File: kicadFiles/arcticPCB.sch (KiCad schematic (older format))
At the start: 174 parts, among them J1 TYPE-C-31-M12_13, J2 Conn_01x06_Male, J3 Conn_01x06_Male, J5 Conn_01x06_Male, SW1 MXSwitch, SW10 MXSwitch, SW11 MXSwitch, SW12 MXSwitch, SW13 MXSwitch, SW14 MXSwitch, SW15 MXSwitch, SW16 MXSwitch, SW17 MXSwitch, SW18 MXSwitch, SW19 MXSwitch, SW2 MXSwitch, SW20 MXSwitch, SW21 MXSwitch, SW22 MXSwitch, SW23 MXSwitch, SW24 MXSwitch, SW25 MXSwitch, SW26 MXSwitch, SW27 MXSwitch, SW28 MXSwitch, SW29 MXSwitch, SW3 MXSwitch, SW30 MXSwitch, SW31 MXSwitch, SW32 MXSwitch, SW33 MXSwitch, SW34 MXSwitch, SW35 MXSwitch, SW36 MXSwitch, SW37 MXSwitch, SW38 MXSwitch, SW39 MXSwitch, SW4 MXSwitch, SW40 MXSwitch, SW41 MXSwitch, SW42 MXSwitch, SW43 MXSwitch, SW44 MXSwitch, SW45 MXSwitch, SW46 MXSwitch, SW47 MXSwitch, SW48 MXSwitch, SW49 MXSwitch, SW5 MXSwitch, SW50 MXSwitch, SW51 MXSwitch, SW52 MXSwitch, SW53 MXSwitch, SW54 MXSwitch, SW55 MXSwitch, SW56 MXSwitch, SW57 MXSwitch, SW58 MXSwitch, SW59 MXSwitch, SW6 MXSwitch, SW60 MXSwitch, SW61 MXSwitch, SW62 MXSwitch, SW63 MXSwitch, SW64 MXSwitch, SW65 MXSwitch, SW7 MXSwitch, SW8 MXSwitch, SW9 MXSwitch, U1 STM32F072-LQFP48, U2 USBLC6-2SC6, U3 MCP1700-3302E_SOT23

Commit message: Add extra pins, organize schematic, add renders
- There were two pins in the PCB that were left unused and un-exposed to use. Now those two pins are broken out so they can be used. To execute this, some cols and rows had to have their pins reallocated.

- Schematic is better organized;

- Added KLE and PCB renders at the REAME file.
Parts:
- added J4: Conn_01x02, Connector_PinHeader_2.54mm:PinHeader_1x02_P2.54mm_Vertical, symbol Connector_Generic:Conn_01x02
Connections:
- net Col10: now also U1.4 (PC15/OSC32_OUT); no longer U1.3 (PC14/OSC32_IN)
- net Col11: now also U1.3 (PC14/OSC32_IN); no longer U1.2 (PC13)
- net Col12: now also U1.2 (PC13); no longer U1.46 (SPI2_NSS/I2S2_WS/I2C1_SDA/TIM17_CH1/PB9)
- net Col13: now also U1.46 (SPI2_NSS/I2S2_WS/I2C1_SDA/TIM17_CH1/PB9); no longer U1.45 (I2C1_SCL/TIM16_CH1/PB8)
- net Col14: now also U1.45 (I2C1_SCL/TIM16_CH1/PB8); no longer U1.43 (2C1_SDA/PB7)
- net Row1: now also U1.43 (2C1_SDA/PB7); no longer U1.42 (I2C1_SCL/PB6)
- net Row2: now also U1.42 (I2C1_SCL/PB6); no longer U1.41 (SPI1_MOSI/I2S1_SD/TIM3_CH2/PB5)
- net J4_2: now reaches U1.40 (SPI1_MISO/I2S1_MCK/TIM3_CH1/PB4)
- net J4_2: now also J4.2 (Pin_2)
- new net J4_1: J4.1 (Pin_1), U1.41 (SPI1_MOSI/I2S1_SD/TIM3_CH2/PB5)
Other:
- note added: "Mounting holes"
- note added: "Switch matrix"
- moved on the sheet: CB1, CB2, CB3, CB4, CB5, CB6, CB7, CB8, H8, L1, L2, L3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

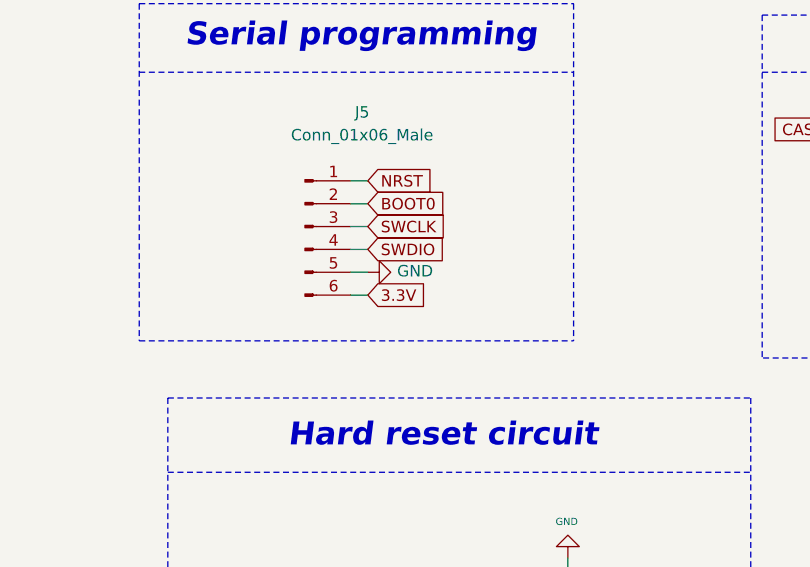
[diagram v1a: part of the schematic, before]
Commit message: Optimize routing, move SWD pins
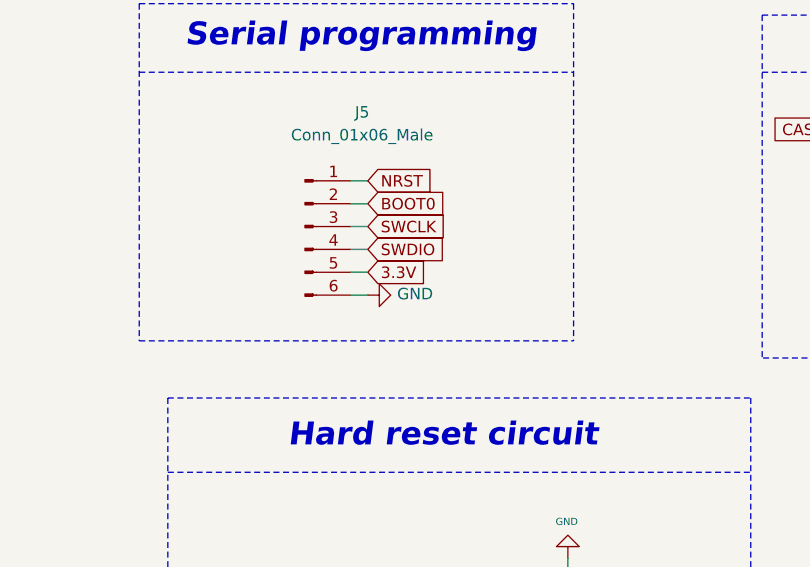
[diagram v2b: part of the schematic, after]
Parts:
- SW1, SW10, SW11, SW12, SW13, SW16, SW17, SW18, SW19, SW2, SW20, SW21, SW22, SW23, SW24, SW25, SW26, SW27, SW3, SW30, SW31, SW32, SW33, SW34, SW35, SW36, SW37, SW38, SW39, SW4, SW40, SW43, SW44, SW45, SW46, SW47, SW48, SW49, SW5, SW50, SW51, SW52, SW55, SW59, SW6, SW61, SW64, SW65, SW7, SW8, SW9: footprint acheron_MX:MX100 -> acheron_MX_SolderMask:MX100
- SW14: footprint acheron_MX:MX200 -> acheron_MX_SolderMask:MX200
- SW15, SW28, SW54, SW56, SW58, SW60: footprint acheron_MX:MX150 -> acheron_MX_SolderMask:MX150
- SW29, SW62: footprint acheron_MX:MX175 -> acheron_MX_SolderMask:MX175
- SW41, SW42: footprint acheron_MX:MX225 -> acheron_MX_SolderMask:MX225
- SW53: footprint acheron_MX:MX275 -> acheron_MX_SolderMask:MX275
- SW57: footprint acheron_MX:MX700R -> acheron_MX_SolderMask:MX700R
- SW63: footprint acheron_MX:MX125 -> acheron_MX_SolderMask:MX125
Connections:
- net 3.3V: now also J5.5 (Pin_5); no longer J5.6 (Pin_6)
- net GND: now also J5.6 (Pin_6); no longer J5.5 (Pin_5)

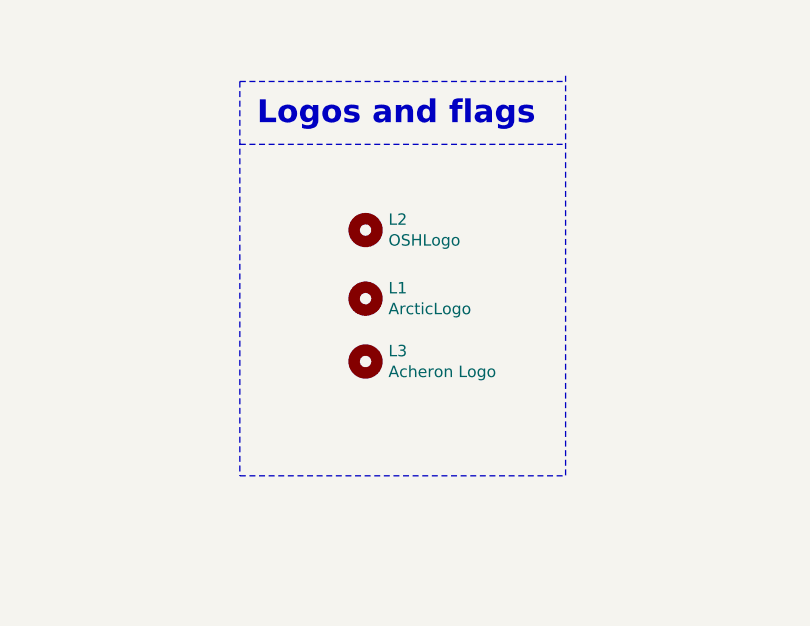
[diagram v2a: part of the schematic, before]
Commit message: Reorganize graphics, optimize routing
- The ./graphics folder was reorganized

- Some traces, specially the ones leading to SWD pins, were re-done for
efficiency and optimization
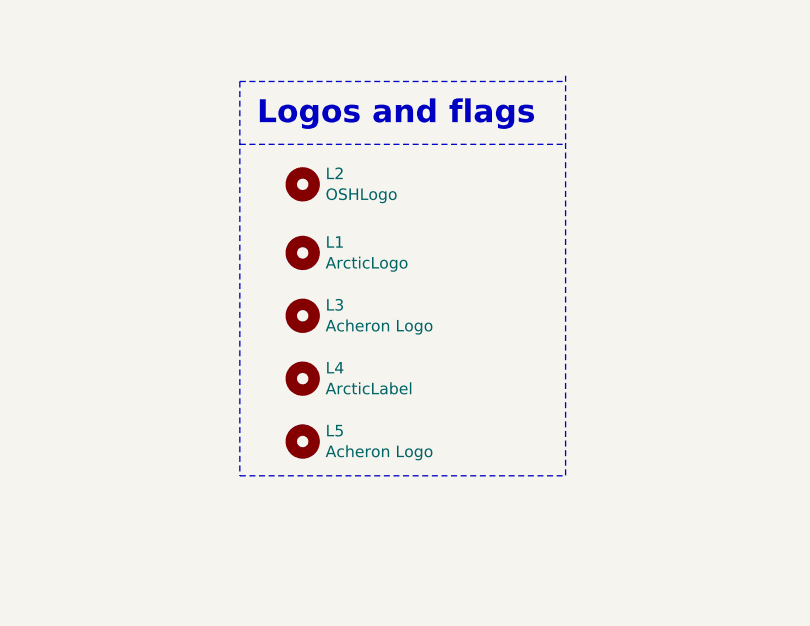
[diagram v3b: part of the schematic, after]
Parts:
- added L4: ArcticLabel, arcticGraphics:arcticLabel, symbol Mechanical:MountingHole
- added L5: Acheron Logo, arcticGraphics:arcticLabelMask, symbol Mechanical:MountingHole
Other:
- moved on the sheet: L1, L2, L3
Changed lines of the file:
@@
 L Mechanical:MountingHole L2
 U 1 1 5C66B5D5
-P 3000 14725
-F 0 "L2" H 3100 14771 50  0000 L CNN
-F 1 "OSHLogo" H 3100 14680 50  0000 L CNN
-F 2 "oshLogo:osh-logo" H 3000 14725 50  0001 C CNN
-F 3 "~" H 3000 14725 50  0001 C CNN
-	1    3000 14725
+P 2725 14525
+F 0 "L2" H 2825 14571 50  0000 L CNN
+F 1 "OSHLogo" H 2825 14480 50  0000 L CNN
+F 2 "oshLogo:osh-logo" H 2725 14525 50  0001 C CNN
+F 3 "~" H 2725 14525 50  0001 C CNN
+	1    2725 14525
 	1    0    0    -1
 $EndComp
@@
 L Mechanical:MountingHole L1
 U 1 1 5D3B6D2E
-P 3000 15025
-F 0 "L1" H 3100 15071 50  0000 L CNN
-F 1 "ArcticLogo" H 3100 14980 50  0000 L CNN
-F 2 "arcticLogo:arcticLogoFilled" H 3000 15025 50  0001 C CNN
-F 3 "~" H 3000 15025 50  0001 C CNN
-	1    3000 15025
+P 2725 14825
+F 0 "L1" H 2825 14871 50  0000 L CNN
+F 1 "ArcticLogo" H 2825 14780 50  0000 L CNN
+F 2 "arcticLogo:arcticLogoFilled" H 2725 14825 50  0001 C CNN
+F 3 "~" H 2725 14825 50  0001 C CNN
+	1    2725 14825
 	1    0    0    -1
 $EndComp
@@
 L Mechanical:MountingHole L3
 U 1 1 5D430F2E
-P 3000 15300
-F 0 "L3" H 3100 15346 50  0000 L CNN
-F 1 "Acheron Logo" H 3100 15255 50  0000 L CNN
-F 2 "acheron_Logos:acheronLong" H 3000 15300 50  0001 C CNN
-F 3 "~" H 3000 15300 50  0001 C CNN
-	1    3000 15300
+P 2725 15100
+F 0 "L3" H 2825 15146 50  0000 L CNN
+F 1 "Acheron Logo" H 2825 15055 50  0000 L CNN
+F 2 "acheron_Logos:acheronLong" H 2725 15100 50  0001 C CNN
+F 3 "~" H 2725 15100 50  0001 C CNN
+	1    2725 15100
 	1    0    0    -1
 $EndComp
@@
 Wire Wire Line
 	22175 16200 22175 16275
+$Comp
+L Mechanical:MountingHole L4
+U 1 1 5D8978A5
+P 2725 15375
+F 0 "L4" H 2825 15421 50  0000 L CNN
+F 1 "ArcticLabel" H 2825 15330 50  0000 L CNN
+F 2 "arcticGraphics:arcticLabel" H 2725 15375 50  0001 C CNN
+F 3 "~" H 2725 15375 50  0001 C CNN
+	1    2725 15375
+	1    0    0    -1
+$EndComp
+$Comp
+L Mechanical:MountingHole L5
+U 1 1 5D8978AB
+P 2725 15650
+F 0 "L5" H 2825 15696 50  0000 L CNN
+F 1 "Acheron Logo" H 2825 15605 50  0000 L CNN
+F 2 "arcticGraphics:arcticLabelMask" H 2725 15650 50  0001 C CNN
+F 3 "~" H 2725 15650 50  0001 C CNN
+	1    2725 15650
+	1    0    0    -1
+$EndComp
 $EndSCHEMATC

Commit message: Update Library, improve footprints and label
- The label  was previously written "release Alpha" which is not the case (this is still version pre-Alpha);

- New MX_SolderMask witch footprints from the AcheronLibrary

- The extra pins were allocated into three symbols (J2, J3 and J4). These were grouped under the same J2, having 14 pins and an improved footprint;

- Optimized routing near the MCU area;

- Added more clearance to the D+/D- differential pair to make sure it is free from interference;
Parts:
- removed J2, J3: Conn_01x06_Male, acheron_Connectors:HEADER_6PIN, symbol Connector:Conn_01x06_Male
- removed J4: Conn_01x02, Connector_PinHeader_2.54mm:PinHeader_1x02_P2.54mm_Vertical, symbol Connector_Generic:Conn_01x02
- added J2: Conn_01x14, Connector_PinHeader_2.54mm:PinHeader_1x14_P2.54mm_Vertical, symbol Connector_Generic:Conn_01x14
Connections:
- net J2_1 renamed Extra8
- net Extra8: now also J2.8 (Pin_8)
- net J2_2 renamed Extra7
- net Extra7: now also J2.7 (Pin_7)
- net J2_3 renamed Extra6
- net Extra6: now also J2.6 (Pin_6)
- net J2_4 renamed Extra5
- net Extra5: now also J2.5 (Pin_5)
- net J2_5 renamed Extra4
- net Extra4: now also J2.4 (Pin_4)
- net J2_6 renamed Extra3
- net Extra3: now also J2.3 (Pin_3)
- net J3_1 renamed Extra14
- net Extra14: now also J2.14 (Pin_14)
- net J3_2 renamed Extra13
- net Extra13: now also J2.13 (Pin_13)
- net J3_3 renamed Extra12
- net Extra12: now also J2.12 (Pin_12)
- net J3_4 renamed Extra11
- net Extra11: now also J2.11 (Pin_11)
- net J3_5 renamed Extra10
- net Extra10: now also J2.10 (Pin_10)
- net J3_6 renamed Extra9
- net Extra9: now also J2.9 (Pin_9)
- net J4_1 renamed Extra1
- net Extra1: now also J2.1 (Pin_1)
- net J4_2 renamed Extra2
- net Extra2: now also J2.2 (Pin_2)
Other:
- moved on the sheet: CRST1, CRST2, CSH1, CSH2, CSI1, CSO1, CUSB1, DF1, DRST1, DS1, DSH1, F1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

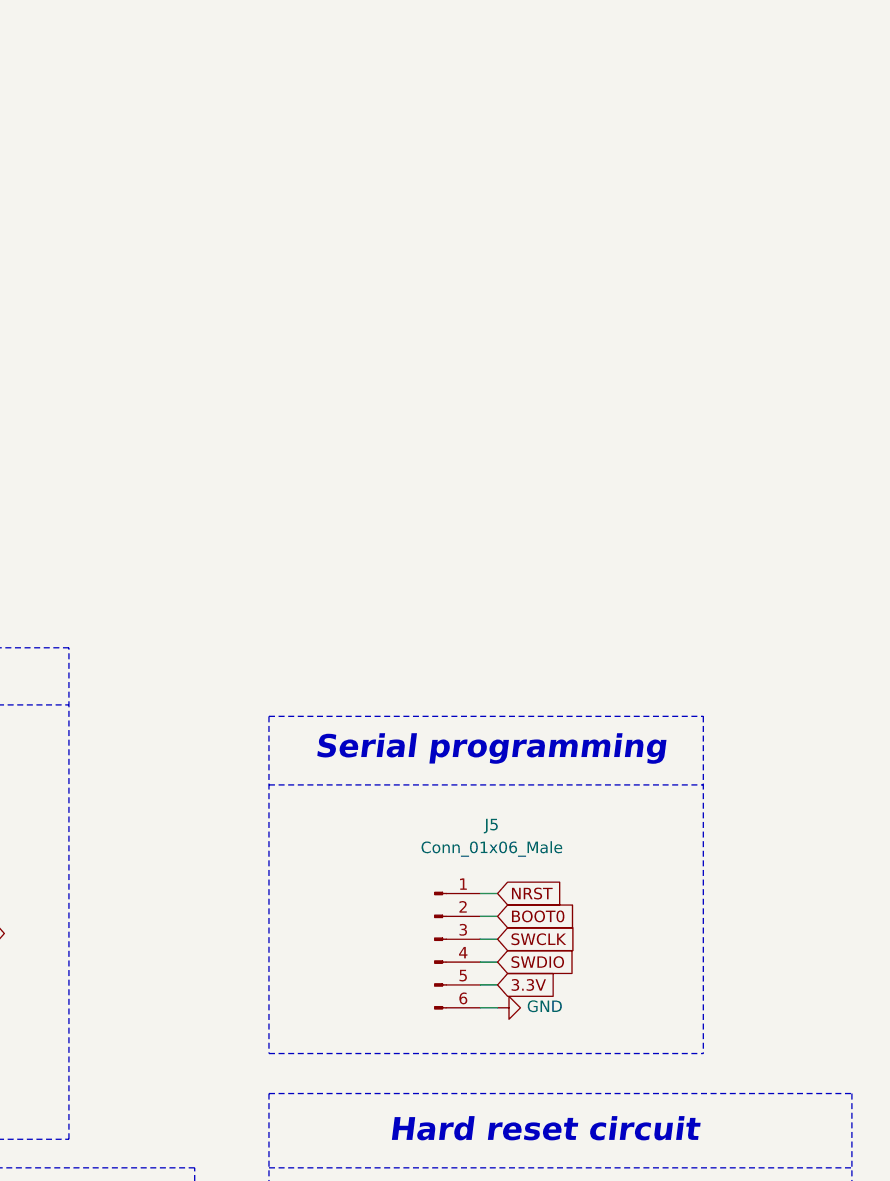
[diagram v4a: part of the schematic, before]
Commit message: Add new pin header footprints
- The AcheronLibrary pin header footprints were updated, and a SWD JTAG
footprint was added (see AcheronLibrary commit 280b825).

- Following this, the pin header footprints on Arctic were redone and
the JTAG footprint was added.
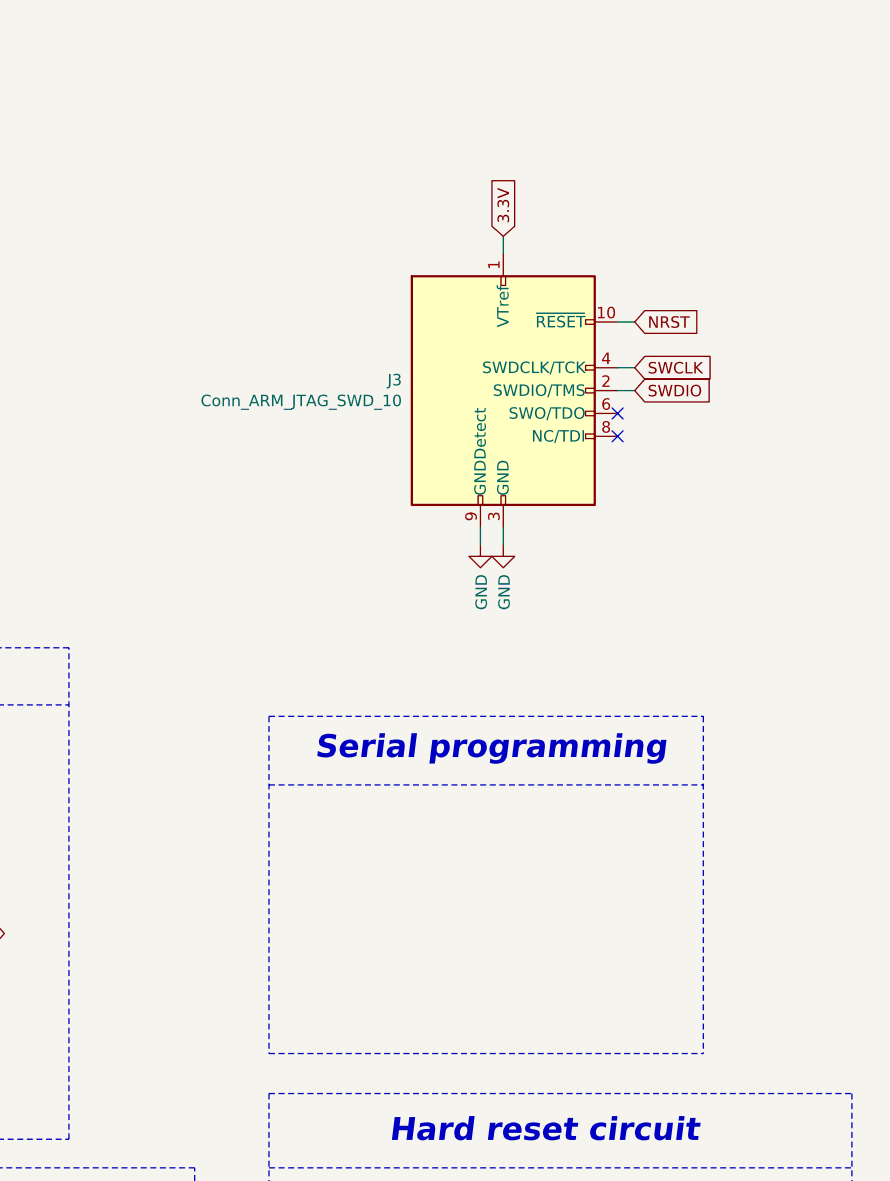
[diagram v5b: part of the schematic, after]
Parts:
- removed J5: Conn_01x06_Male, acheron_Connectors:HEADER_6PIN_HORIZONTAL, symbol Connector:Conn_01x06_Male
- added J3: Conn_ARM_JTAG_SWD_10, acheron_Connectors:Conn_ARM_JTAG_SWD_10, symbol Connector:Conn_ARM_JTAG_SWD_10
- J2: footprint Connector_PinHeader_2.54mm:PinHeader_1x14_P2.54mm_Vertical -> acheron_Connectors:PinHeader_1x14_P2.54mm_Vertical
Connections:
- net 3.3V: now also J3.1 (VTref)
- net GND: now also J3.3 (GND), J3.5 (GND), J3.9 (GNDDetect)
- net NRST: now also J3.10 (~RESET~)
- net SWCLK: now also J3.4 (SWDCLK/TCK)
- net SWDIO: now also J3.2 (SWDIO/TMS)
- no-connect marks 2 -> 4
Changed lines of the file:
@@
 Serial programming
 Wire Wire Line
-	9000 14100 8925 14100
-Text GLabel 9000 14100 2    50   Input ~ 0
+	9600 11600 9525 11600
+Text GLabel 9600 11600 2    50   Input ~ 0
 SWDIO
 Wire Wire Line
-	8925 14300 9000 14300
-Text GLabel 9000 14200 2    50   Input ~ 0
+	9025 12200 9025 12275
+Text GLabel 9025 10925 1    50   Input ~ 0
 3.3V
 Wire Wire Line
-	8925 14200 9000 14200
+	9025 11000 9025 10925
 Wire Wire Line
-	9000 13800 8925 13800
-Text GLabel 9000 13900 2    50   Input ~ 0
-BOOT0
-Text GLabel 9000 13800 2    50   Input ~ 0
+	9600 11300 9525 11300
+Text GLabel 9600 11300 2    50   Input ~ 0
 NRST
-Wire Wire Line
-	8925 13900 9000 13900
 $Comp
 L Transistor_BJT:DTC123J QRST1
@@
 	15925 7450 16925 7450
 Wire Wire Line
-	8925 14000 9000 14000
-Text GLabel 9000 14000 2    50   Input ~ 0
+	9525 11500 9600 11500
+Text GLabel 9600 11500 2    50   Input ~ 0
 SWCLK
 $Comp
-L Connector:Conn_01x06_Male J5
-U 1 1 5CF6EE3E
-P 8725 14000
-F 0 "J5" H 8975 14500 50  0000 C CNN
-F 1 "Conn_01x06_Male" H 8975 14400 50  0000 C CNN
-F 2 "acheron_Connectors:HEADER_6PIN_HORIZONTAL" H 8725 14000 50  0001 C CNN
-F 3 "~" H 8725 14000 50  0001 C CNN
-	1    8725 14000
-	1    0    0    -1
-$EndComp
-$Comp
 L power:GND #PWR0103
 U 1 1 5CFDFC6D
-P 9000 14300
-F 0 "#PWR0103" H 9000 14050 50  0001 C CNN
-F 1 "GND" V 9005 14172 50  0000 R CNN
-F 2 "" H 9000 14300 50  0001 C CNN
-F 3 "" H 9000 14300 50  0001 C CNN
-	1    9000 14300
-	0    -1   -1   0
+P 9025 12275
+F 0 "#PWR0103" H 9025 12025 50  0001 C CNN
+F 1 "GND" V 9030 12147 50  0000 R CNN
+F 2 "" H 9025 12275 50  0001 C CNN
+F 3 "" H 9025 12275 50  0001 C CNN
+	1    9025 12275
+	1    0    0    -1
 $EndComp
 Text GLabel 20425 19775 3    50   Input ~ 0
@@
 F 0 "J2" H 12205 12843 50  0000 L CNN
 F 1 "Conn_01x14" H 12205 12750 50  0000 L CNN
-F 2 "Connector_PinHeader_2.54mm:PinHeader_1x14_P2.54mm_Vertical" H 12125 12850 50  0001 C CNN
+F 2 "acheron_Connectors:PinHeader_1x14_P2.54mm_Vertical" H 12125 12850 50  0001 C CNN
 F 3 "~" H 12125 12850 50  0001 C CNN
 	1    12125 12850
@@
 Wire Wire Line
 	11875 12250 11925 12250
+$Comp
+L Connector:Conn_ARM_JTAG_SWD_10 J3
+U 1 1 5D8D65B1
+P 9025 11600
+F 0 "J3" H 8582 11646 50  0000 R CNN
+F 1 "Conn_ARM_JTAG_SWD_10" H 8582 11555 50  0000 R CNN
+F 2 "acheron_Connectors:Conn_ARM_JTAG_SWD_10" H 9025 11600 50  0001 C CNN
+F 3 "http://infocenter.arm.com/help/topic/com.arm.doc.ddi0314h/DDI0314H_coresight_components_trm.pdf" V 8675 10350 50  0001 C CNN
+	1    9025 11600
+	1    0    0    -1
+$EndComp
+Wire Wire Line
+	8925 12200 8925 12275
+$Comp
+L power:GND #PWR0115
+U 1 1 5D94EDF9
+P 8925 12275
+F 0 "#PWR0115" H 8925 12025 50  0001 C CNN
+F 1 "GND" V 8930 12147 50  0000 R CNN
+F 2 "" H 8925 12275 50  0001 C CNN
+F 3 "" H 8925 12275 50  0001 C CNN
+	1    8925 12275
+	1    0    0    -1
+$EndComp
+NoConn ~ 9525 11700
+NoConn ~ 9525 11800
 $EndSCHEMATC

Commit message: Improved diff. pair pad clearances
- The differential pair D-/D+ has a 20thou clearance, which was used by
KiCad for the pads on USBLC6 (U2) and the microprocessor (U1), making
the filled zones around those pads not so good. The net clearance of
20thou remains, although the pads now have a normal clearance of 6 thou.
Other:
- note added: "Extra pins"
- moved on the sheet: CB1, CB2, CB3, CB4, CB5, CB6, CB7, CB8, CRST1, CRST2, CSH1, CSH2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

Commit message: Update: fixed naming of top row
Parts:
- SW1: value MXSwitch -> ESC
- SW10: value MXSwitch -> 9
- SW11: value MXSwitch -> 0
- SW12: value MXSwitch -> -_
- SW13: value MXSwitch -> +=
- SW14: value MXSwitch -> 2U BKSP
- SW15: value MXSwitch -> TAB_150
- SW16: value MXSwitch -> Q
- SW17: value MXSwitch -> W
- SW18: value MXSwitch -> E
- SW19: value MXSwitch -> R
- SW2: value MXSwitch -> 1
- SW20: value MXSwitch -> T
- SW21: value MXSwitch -> Y
- SW22: value MXSwitch -> U
- SW23: value MXSwitch -> I
- SW24: value MXSwitch -> O
- SW25: value MXSwitch -> P
- SW26: value MXSwitch -> [{
- SW27: value MXSwitch -> ]}
- SW28: value MXSwitch -> \\|_150
- SW29: value MXSwitch -> CAPS_175
- SW3: value MXSwitch -> 2
- SW30: value MXSwitch -> A
- SW31: value MXSwitch -> S
- SW32: value MXSwitch -> D
- SW33: value MXSwitch -> F
- SW34: value MXSwitch -> G
- SW35: value MXSwitch -> H
- SW36: value MXSwitch -> J
- SW37: value MXSwitch -> K
- SW38: value MXSwitch -> L
- SW39: value MXSwitch -> :;
- SW4: value MXSwitch -> 3
- SW40: value MXSwitch -> \"'
- SW41: value MXSwitch -> ENTER_225
- SW42: value MXSwitch -> LSHIFT_225
- SW43: value MXSwitch -> Z
- SW44: value MXSwitch -> X
- SW45: value MXSwitch -> C
- SW46: value MXSwitch -> V
- SW47: value MXSwitch -> B
- SW48: value MXSwitch -> N
- SW49: value MXSwitch -> M
- SW5: value MXSwitch -> 4
- SW50: value MXSwitch -> <,
- SW51: value MXSwitch -> >.
- SW52: value MXSwitch -> ?/
- SW53: value MXSwitch -> RSHIFT_275
- SW54: value MXSwitch -> LCTRL_150
- SW55: value MXSwitch -> LGUI_100
- SW56: value MXSwitch -> LALT_150
- SW57: value MXSwitch -> SPACE_7U
- SW58: value MXSwitch -> RALT_150
- SW59: value MXSwitch -> RGUI_100
- SW6: value MXSwitch -> 5
- SW60: value MXSwitch -> RCTRL_150
- SW61: value MXSwitch -> FN_100
- SW62: value MXSwitch -> RSHIFT_175
- SW63: value MXSwitch -> STEPPED_CAPS_125
- SW64: value MXSwitch -> 1U LBKSP
- SW65: value MXSwitch -> 1U RBKSP
- SW7: value MXSwitch -> 6
- SW8: value MXSwitch -> 7
- SW9: value MXSwitch -> 8
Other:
- note removed: "SW14: 2U backspace"
- note removed: "SW64: 1U left backspace"
- note removed: "SW65: 1U right backspace"

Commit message: Fiz RShift / Enter stab collision issue
- The RShift and Enter stabs were positioned in a way that they would collide. The Enter stab was rotated to avoid this.
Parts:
- SW41: footprint acheron_MX_SolderMask:MX225 -> acheron_MX_SolderMask:MX225R
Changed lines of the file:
@@
 EESchema Schematic File Version 4
-LIBS:arcticPCB-cache
 EELAYER 30 0
 EELAYER END
@@
 F 0 "SW41" H 13975 4675 50  0000 C CNN
 F 1 "ENTER_225" H 13975 4500 40  0000 C CNN
-F 2 "acheron_MX_SolderMask:MX225" H 13975 4625 50  0001 C CNN
+F 2 "acheron_MX_SolderMask:MX225R" H 13975 4625 50  0001 C CNN
 F 3 "" H 13975 4625 50  0001 C CNN
 	1    13975 4625
